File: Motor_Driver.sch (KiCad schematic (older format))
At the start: 13 parts, among them J3 Screw_Terminal_01x02, J4 Screw_Terminal_01x02, J5 Screw_Terminal_01x02, U1 TB67H420FTG_EL

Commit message: Schematic Rev_One Done pre review
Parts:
- removed C14: 100uF, symbol pspice:CAP
- removed C15, C9: .1uF, symbol pspice:CAP
- added C10: .1uF, SamacSys_Parts:CAPC2012X110N, symbol SamacSys_Parts:C0805C104MMREC7210
- added C11: 100uF, SamacSys_Parts:CAPAE1290X1650N, symbol SamacSys_Parts:MAL214699906E3
- added C13: .1uF, SamacSys_Parts:CAPC0603X33N, symbol SamacSys_Parts:GRM033R61C104KE84D
- added R6, R7, R9: .01, SamacSys_Parts:RESC6430X66N, symbol SamacSys_Parts:PCS2512DR0100ET
- C12: renamed from C8; footprint (none) -> Capacitor_SMD:C_0402_1005Metric
- J3, J4, J5: footprint (none) -> Connector_PinHeader_2.54mm:PinHeader_1x02_P2.54mm_Vertical
- R10: renamed from R6; footprint (none) -> Resistor_SMD:R_0402_1005Metric
- R11: renamed from R7; footprint (none) -> Resistor_SMD:R_0402_1005Metric
- R12: renamed from R8; footprint (none) -> Resistor_SMD:R_0402_1005Metric
- R5: renamed from R4; footprint (none) -> Resistor_SMD:R_0402_1005Metric
- R8: renamed from R5; footprint (none) -> Resistor_SMD:R_0402_1005Metric
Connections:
- net labels added: ADC_1, ADC_2, ADC_3, ADC_MUX_GND, ADC_VREFA, ADC_VREFB, MotorA_Neg_Out, MotorA_Pos_Out, MotorB_Pos_Out
- net labels removed: H-BridgeA_GND, H-BridgeB_GND
- wire segments 67 -> 96
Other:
- note added: "By using the current through A_Pos and A_Neg summed together\nyou can get the current through the single motor."
- note added: "Current Sense for M1, M2, and single motor"
- moved on the sheet: C12, R5

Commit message: Layout Rev_One done need to revise to shrink board
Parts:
- J3: value Screw_Terminal_01x02 -> M1
- J4: value Screw_Terminal_01x02 -> M2
- J5: value Screw_Terminal_01x02 -> PWR_IN
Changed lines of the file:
@@
 P 3600 6250
 F 0 "J5" H 3680 6242 50  0000 L CNN
-F 1 "Screw_Terminal_01x02" H 3680 6151 50  0000 L CNN
+F 1 "PWR_IN" H 3680 6151 50  0000 L CNN
 F 2 "Connector_PinHeader_2.54mm:PinHeader_1x02_P2.54mm_Vertical" H 3600 6250 50  0001 C CNN
 F 3 "~" H 3600 6250 50  0001 C CNN
@@
 P 3600 6000
 F 0 "J4" H 3680 5992 50  0000 L CNN
-F 1 "Screw_Terminal_01x02" H 3680 5901 50  0000 L CNN
+F 1 "M2" H 3680 5901 50  0000 L CNN
 F 2 "Connector_PinHeader_2.54mm:PinHeader_1x02_P2.54mm_Vertical" H 3600 6000 50  0001 C CNN
 F 3 "~" H 3600 6000 50  0001 C CNN
@@
 P 3600 5750
 F 0 "J3" H 3680 5742 50  0000 L CNN
-F 1 "Screw_Terminal_01x02" H 3680 5651 50  0000 L CNN
+F 1 "M1" H 3680 5651 50  0000 L CNN
 F 2 "Connector_PinHeader_2.54mm:PinHeader_1x02_P2.54mm_Vertical" H 3600 5750 50  0001 C CNN
 F 3 "~" H 3600 5750 50  0001 C CNN

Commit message: feather profile
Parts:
- removed C11: 100uF, SamacSys_Parts:CAPAE1290X1650N, symbol SamacSys_Parts:MAL214699906E3
- added C11: 100uF, CAPAE660X800N, symbol SamacSys_Parts:EEE-FK1V101XV
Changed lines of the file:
@@
 By using the current through A_Pos and A_Neg summed together\nyou can get the current through the single motor.
-$Comp
-L SamacSys_Parts:MAL214699906E3 C11
-U 1 1 60EC4C3E
-P 1950 5850
-F 0 "C11" V 2154 5980 50  0000 L CNN
-F 1 "100uF" V 2245 5980 50  0000 L CNN
-F 2 "SamacSys_Parts:CAPAE1290X1650N" H 2300 5900 50  0001 L CNN
-F 3 "https://www.vishay.com/docs/28403/146cti.pdf" H 2300 5800 50  0001 L CNN
-F 4 "Vishay Extreme 100uF 100 V Aluminium Electrolytic Capacitor 1216, 146 CTI Series 1500  6000h 12.5 x 12.5 x 16mm" H 2300 5700 50  0001 L CNN "Description"
-F 5 "16.5" H 2300 5600 50  0001 L CNN "Height"
-F 6 "594-MAL214699906E3" H 2300 5500 50  0001 L CNN "Mouser Part Number"
-F 7 "https://www.mouser.co.uk/ProductDetail/Vishay-BC-Components/MAL214699906E3?qs=gUBFJjLdUib9zXP5zbfSLg%3D%3D" H 2300 5400 50  0001 L CNN "Mouser Price/Stock"
-F 8 "Vishay" H 2300 5300 50  0001 L CNN "Manufacturer_Name"
-F 9 "MAL214699906E3" H 2300 5200 50  0001 L CNN "Manufacturer_Part_Number"
-	1    1950 5850
-	0    1    1    0
-$EndComp
-Connection ~ 1950 5850
-Wire Wire Line
-	1950 5850 2300 5850
 $Comp
 L SamacSys_Parts:C0805C104MMREC7210 C10
@@
 	1100 5850 1350 5850
 Connection ~ 1350 5850
-Wire Wire Line
-	1350 5850 1950 5850
 $Comp
 L SamacSys_Parts:GRM033R61C104KE84D C13
@@
 Text GLabel 5200 6750 2    50   Input ~ 0
 TBLKAB
+$Comp
+L SamacSys_Parts:EEE-FK1V101XV C11
+U 1 1 60FCF7A1
+P 1950 5850
+F 0 "C11" V 2154 5980 50  0000 L CNN
+F 1 "100uF" V 2245 5980 50  0000 L CNN
+F 2 "CAPAE660X800N" H 2300 5900 50  0001 L CNN
+F 3 "https://na.industrial.panasonic.com/file-download/3122" H 2300 5800 50  0001 L CNN
+F 4 "Aluminum Electrolytic Capacitors - SMD 35VDC 100uF 20% Anti-Vibe AEC-Q200" H 2300 5700 50  0001 L CNN "Description"
+F 5 "8" H 2300 5600 50  0001 L CNN "Height"
+F 6 "667-EEE-FK1V101XV" H 2300 5500 50  0001 L CNN "Mouser Part Number"
+F 7 "https://www.mouser.co.uk/ProductDetail/Panasonic/EEE-FK1V101XV?qs=PzGy0jfpSMuc2LHnauKjyg%3D%3D" H 2300 5400 50  0001 L CNN "Mouser Price/Stock"
+F 8 "Panasonic" H 2300 5300 50  0001 L CNN "Manufacturer_Name"
+F 9 "EEE-FK1V101XV" H 2300 5200 50  0001 L CNN "Manufacturer_Part_Number"
+	1    1950 5850
+	0    1    1    0
+$EndComp
+Wire Wire Line
+	1350 5850 1950 5850
+Connection ~ 1950 5850
+Wire Wire Line
+	1950 5850 2300 5850
 $EndSCHEMATC

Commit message: Remote work
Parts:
- C10: symbol SamacSys_Parts:C0805C104MMREC7210 -> ESC_5A-rescue:C0805C104MMREC7210-SamacSys_Parts
- C11: symbol SamacSys_Parts:EEE-FK1V101XV -> ESC_5A-rescue:EEE-FK1V101XV-SamacSys_Parts
- C13: symbol SamacSys_Parts:GRM033R61C104KE84D -> ESC_5A-rescue:GRM033R61C104KE84D-SamacSys_Parts
- R6, R7, R9: symbol SamacSys_Parts:PCS2512DR0100ET -> ESC_5A-rescue:PCS2512DR0100ET-SamacSys_Parts
- U1: symbol 2021-06-21_15-40-13:TB67H420FTG_EL -> ESC_5A-rescue:TB67H420FTG_EL-2021-06-21_15-40-13
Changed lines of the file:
@@
 $EndDescr
 $Comp
-L 2021-06-21_15-40-13:TB67H420FTG_EL U?
+L ESC_5A-rescue:TB67H420FTG_EL-2021-06-21_15-40-13 U?
 U 1 1 60E1079C
 P 1950 3950
@@
 $EndComp
 $Comp
-L 2021-06-21_15-40-13:TB67H420FTG_EL U?
+L ESC_5A-rescue:TB67H420FTG_EL-2021-06-21_15-40-13 U?
 U 2 1 60E107A2
 P 5300 3400
@@
 Motor Driver Power
 $Comp
-L SamacSys_Parts:PCS2512DR0100ET R7
+L ESC_5A-rescue:PCS2512DR0100ET-SamacSys_Parts R7
 U 1 1 60D7DF2B
 P 1600 2450
@@
 MotorB_Pos
 $Comp
-L SamacSys_Parts:PCS2512DR0100ET R6
+L ESC_5A-rescue:PCS2512DR0100ET-SamacSys_Parts R6
 U 1 1 60D7DF37
 P 1600 2100
@@
 Current Sense for M1, M2, and single motor
 $Comp
-L SamacSys_Parts:PCS2512DR0100ET R9
+L ESC_5A-rescue:PCS2512DR0100ET-SamacSys_Parts R9
 U 1 1 60DD4ABF
 P 4050 2100
@@
 By using the current through A_Pos and A_Neg summed together\nyou can get the current through the single motor.
 $Comp
-L SamacSys_Parts:C0805C104MMREC7210 C10
+L ESC_5A-rescue:C0805C104MMREC7210-SamacSys_Parts C10
 U 1 1 60ED41BF
 P 1350 5850
@@
 Connection ~ 1350 5850
 $Comp
-L SamacSys_Parts:GRM033R61C104KE84D C13
+L ESC_5A-rescue:GRM033R61C104KE84D-SamacSys_Parts C13
 U 1 1 60F0446C
 P 5200 7300
@@
 TBLKAB
 $Comp
-L SamacSys_Parts:EEE-FK1V101XV C11
+L ESC_5A-rescue:EEE-FK1V101XV-SamacSys_Parts C11
 U 1 1 60FCF7A1
 P 1950 5850

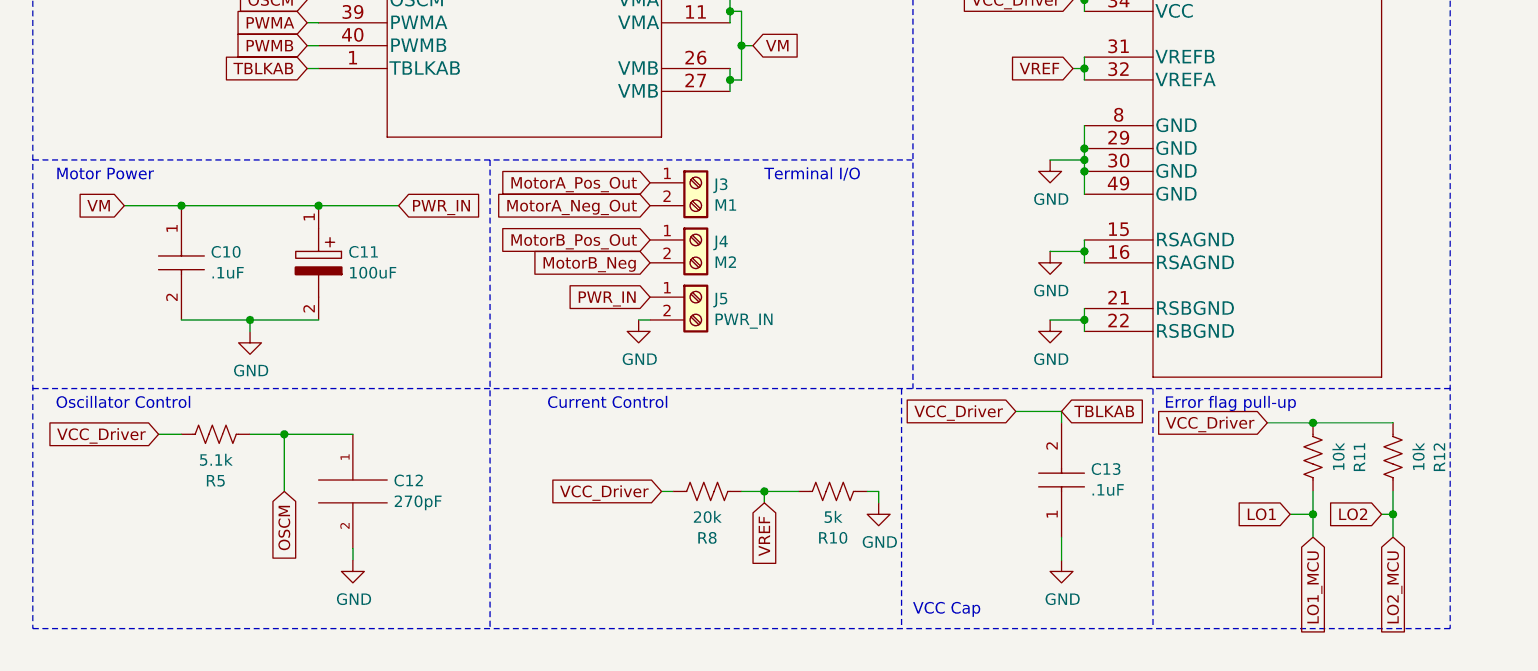
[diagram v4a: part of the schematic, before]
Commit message: Converted everything to XT30
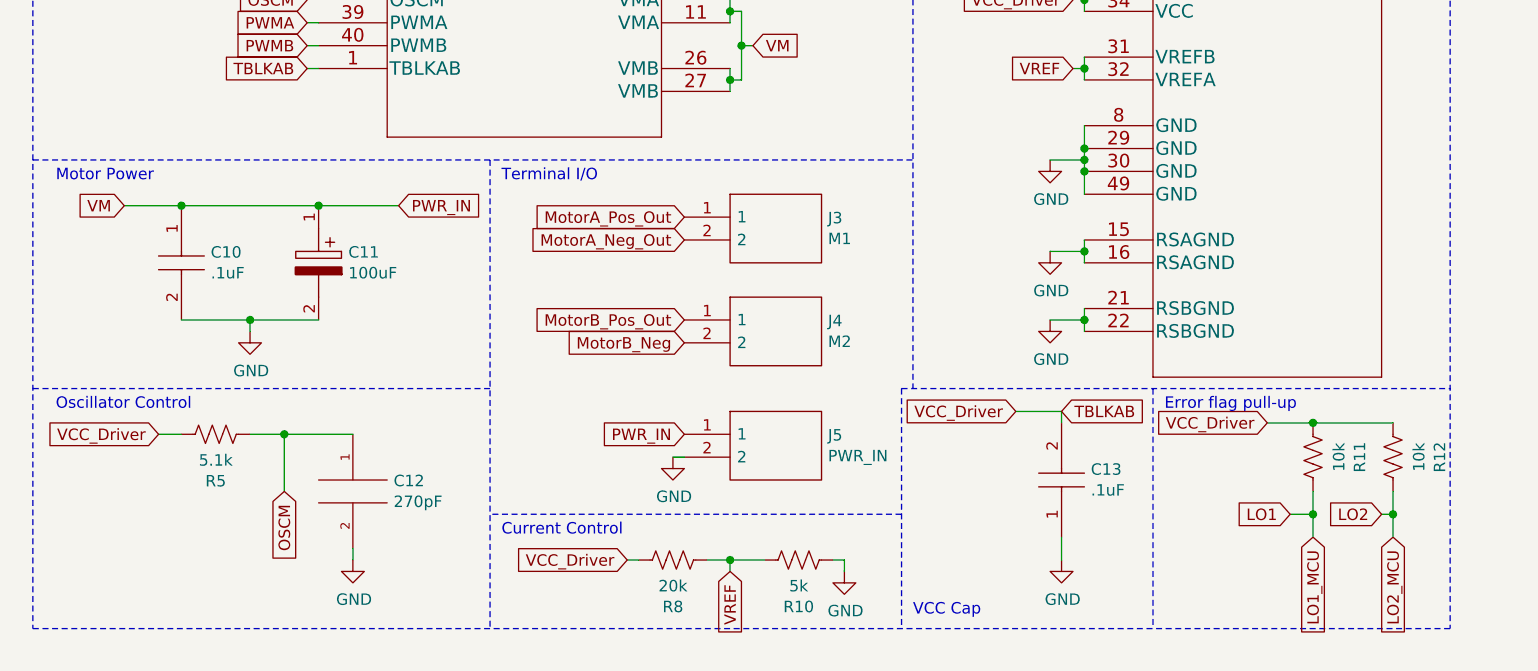
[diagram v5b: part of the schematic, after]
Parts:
- removed J3: M1, Connector_PinHeader_2.54mm:PinHeader_1x02_P2.54mm_Vertical, symbol Connector:Screw_Terminal_01x02
- removed J4: M2, Connector_PinHeader_2.54mm:PinHeader_1x02_P2.54mm_Vertical, symbol Connector:Screw_Terminal_01x02
- removed J5: PWR_IN, Connector_PinHeader_2.54mm:PinHeader_1x02_P2.54mm_Vertical, symbol Connector:Screw_Terminal_01x02
- added J3: M1, XT30PB, symbol SamacSys_Parts:XT30PB
- added J4: M2, XT30PB, symbol SamacSys_Parts:XT30PB
- added J5: PWR_IN, XT30PB, symbol SamacSys_Parts:XT30PB
- C11: footprint CAPAE660X800N -> SamacSys_Parts:CAPAE660X800N
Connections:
- net ADC_1: now also J3.1
- net ADC_2: now also J4.1
- net ADC_3: now also J3.2
- net GND: now also J5.2
- net MotorB_Neg: now also J4.2
- net PWR_IN: now also J5.1
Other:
- moved on the sheet: R10, R8
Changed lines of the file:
@@
 L Device:R_US R?
 U 1 1 60EAD954
-P 4200 7100
+P 4050 7400
 AR Path="/60EAD954" Ref="R?"  Part="1"
 AR Path="/60E06626/60EAD954" Ref="R10"  Part="1"
-F 0 "R10" V 4405 7100 50  0000 C CNN
-F 1 "5k" V 4314 7100 50  0000 C CNN
-F 2 "Resistor_SMD:R_0402_1005Metric" V 4240 7090 50  0001 C CNN
-F 3 "~" H 4200 7100 50  0001 C CNN
-	1    4200 7100
+F 0 "R10" V 4255 7400 50  0000 C CNN
+F 1 "5k" V 4164 7400 50  0000 C CNN
+F 2 "Resistor_SMD:R_0402_1005Metric" V 4090 7390 50  0001 C CNN
+F 3 "~" H 4050 7400 50  0001 C CNN
+	1    4050 7400
 	0    1    1    0
 $EndComp
@@
 L Device:R_US R?
 U 1 1 60EAD95A
-P 3650 7100
+P 3500 7400
 AR Path="/60EAD95A" Ref="R?"  Part="1"
 AR Path="/60E06626/60EAD95A" Ref="R8"  Part="1"
-F 0 "R8" V 3855 7100 50  0000 C CNN
-F 1 "20k" V 3764 7100 50  0000 C CNN
-F 2 "Resistor_SMD:R_0402_1005Metric" V 3690 7090 50  0001 C CNN
-F 3 "~" H 3650 7100 50  0001 C CNN
-	1    3650 7100
+F 0 "R8" V 3705 7400 50  0000 C CNN
+F 1 "20k" V 3614 7400 50  0000 C CNN
+F 2 "Resistor_SMD:R_0402_1005Metric" V 3540 7390 50  0001 C CNN
+F 3 "~" H 3500 7400 50  0001 C CNN
+	1    3500 7400
 	0    1    1    0
 $EndComp
 Wire Wire Line
-	4350 7100 4400 7100
-Wire Wire Line
-	4400 7150 4400 7100
+	4200 7400 4250 7400
+Wire Wire Line
+	4250 7450 4250 7400
 $Comp
 L power:GND #PWR?
 U 1 1 60EAD965
-P 4400 7150
+P 4250 7450
 AR Path="/60EAD965" Ref="#PWR?"  Part="1"
 AR Path="/60E06626/60EAD965" Ref="#PWR030"  Part="1"
-F 0 "#PWR030" H 4400 6900 50  0001 C CNN
-F 1 "GND" H 4405 6977 50  0000 C CNN
-F 2 "" H 4400 7150 50  0001 C CNN
-F 3 "" H 4400 7150 50  0001 C CNN
-	1    4400 7150
-	1    0    0    -1
-$EndComp
-Text GLabel 3450 7100 0    50   Input ~ 0
+F 0 "#PWR030" H 4250 7200 50  0001 C CNN
+F 1 "GND" H 4255 7277 50  0000 C CNN
+F 2 "" H 4250 7450 50  0001 C CNN
+F 3 "" H 4250 7450 50  0001 C CNN
+	1    4250 7450
+	1    0    0    -1
+$EndComp
+Text GLabel 3300 7400 0    50   Input ~ 0
 VCC_Driver
 Text GLabel 5250 4950 0    50   Input ~ 0
 VCC_Driver
-Text GLabel 3900 7150 3    50   Input ~ 0
+Text GLabel 3750 7450 3    50   Input ~ 0
 VREF
 Wire Wire Line
-	3800 7100 3900 7100
-Wire Wire Line
-	3900 7100 3900 7150
-Connection ~ 3900 7100
-Wire Wire Line
-	3900 7100 4050 7100
+	3650 7400 3750 7400
+Wire Wire Line
+	3750 7400 3750 7450
+Connection ~ 3750 7400
+Wire Wire Line
+	3750 7400 3900 7400
 Text GLabel 5000 6750 0    50   Input ~ 0
 VCC_Driver
@@
 $EndComp
 Wire Wire Line
-	3500 7100 3450 7100
+	3350 7400 3300 7400
 Wire Wire Line
 	5200 6800 5200 6750
@@
 Text Notes 800  6750 0    50   ~ 0
 Oscillator Control
-Text Notes 2950 6750 0    50   ~ 0
+Text Notes 2750 7300 0    50   ~ 0
 Current Control
 Text Notes 4550 7650 0    50   ~ 0
@@
 Text Notes 800  5750 0    50   ~ 0
 Motor Power
-$Comp
-L Connector:Screw_Terminal_01x02 J5
-U 1 1 60FD2C43
-P 3600 6250
-F 0 "J5" H 3680 6242 50  0000 L CNN
-F 1 "PWR_IN" H 3680 6151 50  0000 L CNN
-F 2 "Connector_PinHeader_2.54mm:PinHeader_1x02_P2.54mm_Vertical" H 3600 6250 50  0001 C CNN
-F 3 "~" H 3600 6250 50  0001 C CNN
-	1    3600 6250
-	1    0    0    -1
-$EndComp
-$Comp
-L Connector:Screw_Terminal_01x02 J4
-U 1 1 60FD3643
-P 3600 6000
-F 0 "J4" H 3680 5992 50  0000 L CNN
-F 1 "M2" H 3680 5901 50  0000 L CNN
-F 2 "Connector_PinHeader_2.54mm:PinHeader_1x02_P2.54mm_Vertical" H 3600 6000 50  0001 C CNN
-F 3 "~" H 3600 6000 50  0001 C CNN
-	1    3600 6000
-	1    0    0    -1
-$EndComp
-$Comp
-L Connector:Screw_Terminal_01x02 J3
-U 1 1 60FD4AF3
-P 3600 5750
-F 0 "J3" H 3680 5742 50  0000 L CNN
-F 1 "M1" H 3680 5651 50  0000 L CNN
-F 2 "Connector_PinHeader_2.54mm:PinHeader_1x02_P2.54mm_Vertical" H 3600 5750 50  0001 C CNN
-F 3 "~" H 3600 5750 50  0001 C CNN
-	1    3600 5750
-	1    0    0    -1
-$EndComp
-Text GLabel 3400 5750 0    50   Input ~ 0
+Text GLabel 3550 5900 0    50   Input ~ 0
 MotorA_Pos_Out
-Text GLabel 3400 5850 0    50   Input ~ 0
+Text GLabel 3550 6000 0    50   Input ~ 0
 MotorA_Neg_Out
-Text GLabel 3400 6000 0    50   Input ~ 0
+Text GLabel 3550 6350 0    50   Input ~ 0
 MotorB_Pos_Out
-Text GLabel 3400 6100 0    50   Input ~ 0
+Text GLabel 3550 6450 0    50   Input ~ 0
 MotorB_Neg
-Text GLabel 3400 6250 0    50   Input ~ 0
+Text GLabel 3550 6850 0    50   Input ~ 0
 PWR_IN
 $Comp
 L power:GND #PWR?
 U 1 1 60FE14A5
-P 3350 6350
+P 3500 6950
 AR Path="/60FE14A5" Ref="#PWR?"  Part="1"
 AR Path="/60E06626/60FE14A5" Ref="#PWR029"  Part="1"
-F 0 "#PWR029" H 3350 6100 50  0001 C CNN
-F 1 "GND" H 3355 6177 50  0000 C CNN
-F 2 "" H 3350 6350 50  0001 C CNN
-F 3 "" H 3350 6350 50  0001 C CNN
-	1    3350 6350
-	1    0    0    -1
-$EndComp
-Wire Wire Line
-	3400 6350 3350 6350
-Text Notes 3900 5750 0    50   ~ 0
-Terminal I/O
+F 0 "#PWR029" H 3500 6700 50  0001 C CNN
+F 1 "GND" H 3505 6777 50  0000 C CNN
+F 2 "" H 3500 6950 50  0001 C CNN
+F 3 "" H 3500 6950 50  0001 C CNN
+	1    3500 6950
+	1    0    0    -1
+$EndComp
+Wire Wire Line
+	3550 6950 3500 6950
 Text Notes 2500 3200 0    50   ~ 0
 Motor Driver control
@@
 Text GLabel 2500 2450 2    50   Input ~ 0
 MotorA_Pos_Out
-Wire Notes Line
-	700  6650 6900 6650
 Wire Notes Line
 	700  5650 4550 5650
@@
 F 0 "C11" V 2154 5980 50  0000 L CNN
 F 1 "100uF" V 2245 5980 50  0000 L CNN
-F 2 "CAPAE660X800N" H 2300 5900 50  0001 L CNN
+F 2 "SamacSys_Parts:CAPAE660X800N" H 2300 5900 50  0001 L CNN
 F 3 "https://na.industrial.panasonic.com/file-download/3122" H 2300 5800 50  0001 L CNN
 F 4 "Aluminum Electrolytic Capacitors - SMD 35VDC 100uF 20% Anti-Vibe AEC-Q200" H 2300 5700 50  0001 L CNN "Description"
@@
 Wire Wire Line
 	1950 5850 2300 5850
+Wire Notes Line
+	4500 6650 6900 6650
+Wire Notes Line
+	700  6650 2700 6650
+Wire Notes Line
+	4500 7200 2700 7200
+Text Notes 2750 5750 0    50   ~ 0
+Terminal I/O
+$Comp
+L SamacSys_Parts:XT30PB J3
+U 1 1 60E6854C
+P 3550 5900
+F 0 "J3" H 4178 5896 50  0000 L CNN
+F 1 "M1" H 4178 5805 50  0000 L CNN
+F 2 "XT30PB" H 4200 6000 50  0001 L CNN
+F 3 "https://www.tme.eu/Document/4acc913878197f8c2e30d4b8cdc47230/XT30UPB%20SPEC.pdf" H 4200 5900 50  0001 L CNN
+F 4 "Mini XT60 XT30 Connector for RC Multirotor Racing Drone Quadcopter" H 4200 5800 50  0001 L CNN "Description"
+F 5 "10.7" H 4200 5700 50  0001 L CNN "Height"
+F 6 "" H 4200 5600 50  0001 L CNN "Mouser Part Number"
+F 7 "" H 4200 5500 50  0001 L CNN "Mouser Price/Stock"
+F 8 "Amass" H 4200 5400 50  0001 L CNN "Manufacturer_Name"
+F 9 "XT30PB" H 4200 5300 50  0001 L CNN "Manufacturer_Part_Number"
+	1    3550 5900
+	1    0    0    -1
+$EndComp
+$Comp
+L SamacSys_Parts:XT30PB J4
+U 1 1 60E68DD0
+P 3550 6350
+F 0 "J4" H 4178 6346 50  0000 L CNN
+F 1 "M2" H 4178 6255 50  0000 L CNN
+F 2 "XT30PB" H 4200 6450 50  0001 L CNN
+F 3 "https://www.tme.eu/Document/4acc913878197f8c2e30d4b8cdc47230/XT30UPB%20SPEC.pdf" H 4200 6350 50  0001 L CNN
+F 4 "Mini XT60 XT30 Connector for RC Multirotor Racing Drone Quadcopter" H 4200 6250 50  0001 L CNN "Description"
+F 5 "10.7" H 4200 6150 50  0001 L CNN "Height"
+F 6 "" H 4200 6050 50  0001 L CNN "Mouser Part Number"
+F 7 "" H 4200 5950 50  0001 L CNN "Mouser Price/Stock"
+F 8 "Amass" H 4200 5850 50  0001 L CNN "Manufacturer_Name"
+F 9 "XT30PB" H 4200 5750 50  0001 L CNN "Manufacturer_Part_Number"
+	1    3550 6350
+	1    0    0    -1
+$EndComp
+$Comp
+L SamacSys_Parts:XT30PB J5
+U 1 1 60E6BAFF
+P 3550 6850
+F 0 "J5" H 4178 6846 50  0000 L CNN
+F 1 "PWR_IN" H 4178 6755 50  0000 L CNN
+F 2 "XT30PB" H 4200 6950 50  0001 L CNN
+F 3 "https://www.tme.eu/Document/4acc913878197f8c2e30d4b8cdc47230/XT30UPB%20SPEC.pdf" H 4200 6850 50  0001 L CNN
+F 4 "Mini XT60 XT30 Connector for RC Multirotor Racing Drone Quadcopter" H 4200 6750 50  0001 L CNN "Description"
+F 5 "10.7" H 4200 6650 50  0001 L CNN "Height"
+F 6 "" H 4200 6550 50  0001 L CNN "Mouser Part Number"
+F 7 "" H 4200 6450 50  0001 L CNN "Mouser Price/Stock"
+F 8 "Amass" H 4200 6350 50  0001 L CNN "Manufacturer_Name"
+F 9 "XT30PB" H 4200 6250 50  0001 L CNN "Manufacturer_Part_Number"
+	1    3550 6850
+	1    0    0    -1
+$EndComp
 $EndSCHEMATC

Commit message: Pre_layout
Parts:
- J3, J4, J5: footprint XT30PB -> Connector_AMASS:AMASS_XT30U-M_1x02_P5.0mm_Vertical
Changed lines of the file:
@@
 F 0 "J3" H 4178 5896 50  0000 L CNN
 F 1 "M1" H 4178 5805 50  0000 L CNN
-F 2 "XT30PB" H 4200 6000 50  0001 L CNN
+F 2 "Connector_AMASS:AMASS_XT30U-M_1x02_P5.0mm_Vertical" H 4200 6000 50  0001 L CNN
 F 3 "https://www.tme.eu/Document/4acc913878197f8c2e30d4b8cdc47230/XT30UPB%20SPEC.pdf" H 4200 5900 50  0001 L CNN
 F 4 "Mini XT60 XT30 Connector for RC Multirotor Racing Drone Quadcopter" H 4200 5800 50  0001 L CNN "Description"
@@
 F 0 "J4" H 4178 6346 50  0000 L CNN
 F 1 "M2" H 4178 6255 50  0000 L CNN
-F 2 "XT30PB" H 4200 6450 50  0001 L CNN
+F 2 "Connector_AMASS:AMASS_XT30U-M_1x02_P5.0mm_Vertical" H 4200 6450 50  0001 L CNN
 F 3 "https://www.tme.eu/Document/4acc913878197f8c2e30d4b8cdc47230/XT30UPB%20SPEC.pdf" H 4200 6350 50  0001 L CNN
 F 4 "Mini XT60 XT30 Connector for RC Multirotor Racing Drone Quadcopter" H 4200 6250 50  0001 L CNN "Description"
@@
 F 0 "J5" H 4178 6846 50  0000 L CNN
 F 1 "PWR_IN" H 4178 6755 50  0000 L CNN
-F 2 "XT30PB" H 4200 6950 50  0001 L CNN
+F 2 "Connector_AMASS:AMASS_XT30U-M_1x02_P5.0mm_Vertical" H 4200 6950 50  0001 L CNN
 F 3 "https://www.tme.eu/Document/4acc913878197f8c2e30d4b8cdc47230/XT30UPB%20SPEC.pdf" H 4200 6850 50  0001 L CNN
 F 4 "Mini XT60 XT30 Connector for RC Multirotor Racing Drone Quadcopter" H 4200 6750 50  0001 L CNN "Description"

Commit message: Layout Rev_One done pre review
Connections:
- net PWR_IN: no longer C10.1, C11.1, U1.10 (VMA), U1.11 (VMA), U1.26 (VMB), U1.27 (VMB)
- new net PWR: C10.1, C11.1, U1.10 (VMA), U1.11 (VMA), U1.26 (VMB), U1.27 (VMB)
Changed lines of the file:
@@
 	1    0    0    -1
 $EndComp
-Text GLabel 2300 5850 2    50   Input ~ 0
-PWR_IN
 Wire Wire Line
 	3750 3850 3750 3900
@@
 	1    0    0    -1
 $EndComp
+Text GLabel 2300 5850 2    50   Input ~ 0
+PWR
 $EndSCHEMATC
